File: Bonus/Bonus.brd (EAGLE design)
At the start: 63.5 x 63.5 mm, 63 parts, among them U1 CD4094BPW, U2 CD4094BPW, U3 CD4094BPW, U4 MPU-9250

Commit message: Fixed bug in bonus PCB
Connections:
- net SPI-MISO: now also MSP430.14; no longer MSP430.15
- net SPI-MOSI: now also MSP430.15; no longer MSP430.14
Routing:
- net SPI-CLK: track 17.9 -> 19.2 mm
- net ACCEL-CS: track 22.4 -> 23.7 mm
- net SPI-MOSI: track 13.7 -> 14.7 mm, vias 0 -> 2
- net SPI-MISO: track 21.6 -> 20.9 mm
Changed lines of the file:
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@@
 <?xml version="1.0" encoding="utf-8"?>
 <!DOCTYPE eagle SYSTEM "eagle.dtd">
-<eagle version="8.5.0">
+<eagle version="9.1.2">
 <drawing>
 <settings>
@@
 </class>
 </classes>
-<designrules name="SeeedStudio_2layer_DRU_no_angle_20140221">
+<designrules name="Seeed_DRU">
 <description language="de">&lt;b&gt;EAGLE Design Rules&lt;/b&gt;
 &lt;p&gt;
@@
 <param name="checkStop" value="0"/>
 <param name="checkValues" value="0"/>
+<param name="checkNames" value="1"/>
+<param name="checkWireStubs" value="1"/>
+<param name="checkPolygonWidth" value="0"/>
 <param name="useDiameter" value="13"/>
 <param name="maxErrors" value="50"/>
@@
 <wire x1="30.947" y1="43.983" x2="30.988" y2="43.942" width="0.1524" layer="1"/>
 <wire x1="30.988" y1="43.942" x2="30.988" y2="40.132" width="0.1524" layer="1"/>
-<wire x1="35.052" y1="33.02" x2="34.382" y2="32.35" width="0.1524" layer="1"/>
+<wire x1="36.576" y1="34.544" x2="34.382" y2="32.35" width="0.1524" layer="1"/>
 <wire x1="34.798" y1="39.624" x2="32.258" y2="39.624" width="0.1524" layer="16"/>
 <via x="34.798" y="39.624" extent="1-16" drill="0.35"/>
@@
 <wire x1="30.988" y1="40.132" x2="31.496" y2="39.624" width="0.1524" layer="1"/>
 <wire x1="31.496" y1="39.624" x2="32.258" y2="39.624" width="0.1524" layer="1"/>
-<wire x1="34.798" y1="39.624" x2="35.052" y2="39.37" width="0.1524" layer="1"/>
-<wire x1="35.052" y1="39.37" x2="35.052" y2="33.02" width="0.1524" layer="1"/>
+<wire x1="34.798" y1="39.624" x2="36.576" y2="37.846" width="0.1524" layer="1"/>
+<wire x1="36.576" y1="37.846" x2="36.576" y2="34.544" width="0.1524" layer="1"/>
 </signal>
 <signal name="BUTTON">
@@
 </signal>
 <signal name="SPI-MISO">
-<contactref element="MSP430" pad="15"/>
 <contactref element="U4" pad="9"/>
 <wire x1="30.15" y1="31.95" x2="29.156" y2="31.95" width="0.1524" layer="1"/>
 <wire x1="29.156" y1="31.95" x2="28.956" y2="31.75" width="0.1524" layer="1"/>
 <wire x1="28.956" y1="31.75" x2="27.94" y2="31.75" width="0.1524" layer="1"/>
-<wire x1="35.412" y1="44.633" x2="33.965" y2="44.633" width="0.1524" layer="1"/>
-<wire x1="33.528" y1="38.862" x2="33.528" y2="44.196" width="0.1524" layer="1"/>
-<wire x1="33.965" y1="44.633" x2="33.528" y2="44.196" width="0.1524" layer="1"/>
 <wire x1="27.94" y1="37.592" x2="28.448" y2="38.1" width="0.1524" layer="1"/>
 <wire x1="27.94" y1="31.75" x2="27.94" y2="37.592" width="0.1524" layer="1"/>
 <wire x1="32.766" y1="38.1" x2="33.528" y2="38.862" width="0.1524" layer="1"/>
 <wire x1="28.448" y1="38.1" x2="32.766" y2="38.1" width="0.1524" layer="1"/>
+<contactref element="MSP430" pad="14"/>
+<wire x1="33.528" y1="43.434" x2="33.528" y2="38.862" width="0.1524" layer="1"/>
+<wire x1="35.412" y1="43.983" x2="34.077" y2="43.983" width="0.1524" layer="1"/>
+<wire x1="34.077" y1="43.983" x2="33.528" y2="43.434" width="0.1524" layer="1"/>
 </signal>
 <signal name="SPI-MOSI">
-<contactref element="MSP430" pad="14"/>
 <contactref element="U4" pad="24"/>
 <wire x1="33.35" y1="32.75" x2="34.02" y2="32.75" width="0.1524" layer="1"/>
-<wire x1="34.544" y1="33.274" x2="34.02" y2="32.75" width="0.1524" layer="1"/>
-<wire x1="35.412" y1="43.983" x2="34.077" y2="43.983" width="0.1524" layer="1"/>
-<wire x1="34.077" y1="43.983" x2="34.036" y2="43.942" width="0.1524" layer="1"/>
-<wire x1="34.036" y1="43.942" x2="34.036" y2="38.608" width="0.1524" layer="1"/>
-<wire x1="34.036" y1="38.608" x2="34.544" y2="38.1" width="0.1524" layer="1"/>
-<wire x1="34.544" y1="38.1" x2="34.544" y2="33.274" width="0.1524" layer="1"/>
+<contactref element="MSP430" pad="15"/>
+<wire x1="35.412" y1="44.633" x2="36.139" y2="44.633" width="0.1524" layer="1"/>
+<wire x1="36.139" y1="44.633" x2="36.83" y2="43.942" width="0.1524" layer="1"/>
+<wire x1="36.83" y1="43.18" x2="36.83" y2="43.942" width="0.1524" layer="16"/>
+<via x="36.83" y="43.942" extent="1-16" drill="0.35"/>
+<wire x1="35.56" y1="37.084" x2="36.068" y2="37.592" width="0.1524" layer="16"/>
+<via x="35.56" y="37.084" extent="1-16" drill="0.35"/>
+<wire x1="35.56" y1="34.29" x2="35.56" y2="37.084" width="0.1524" layer="1"/>
+<wire x1="34.02" y1="32.75" x2="35.56" y2="34.29" width="0.1524" layer="1"/>
+<wire x1="36.068" y1="37.592" x2="36.068" y2="37.592" width="0.1524" layer="16"/>
+<wire x1="36.068" y1="37.592" x2="36.068" y2="42.418" width="0.1524" layer="16"/>
+<wire x1="36.068" y1="42.418" x2="36.83" y2="43.18" width="0.1524" layer="16"/>
 </signal>
 <signal name="N$7">
@@
 <contactref element="MSP430" pad="19"/>
 <wire x1="35.412" y1="47.2329" x2="34.0249" y2="47.2329" width="0.1524" layer="1"/>
-<wire x1="34.998" y1="31.95" x2="35.56" y2="32.512" width="0.1524" layer="1"/>
-<wire x1="35.56" y1="40.64" x2="35.306" y2="40.894" width="0.1524" layer="1"/>
+<wire x1="34.998" y1="31.95" x2="37.084" y2="34.036" width="0.1524" layer="1"/>
+<wire x1="37.084" y1="39.116" x2="35.306" y2="40.894" width="0.1524" layer="1"/>
 <wire x1="35.306" y1="40.894" x2="32.258" y2="40.894" width="0.1524" layer="16"/>
-<wire x1="35.56" y1="32.512" x2="35.56" y2="40.64" width="0.1524" layer="1"/>
 <via x="35.306" y="40.894" extent="1-16" drill="0.35"/>
 <via x="32.258" y="40.894" extent="1-16" drill="0.35"/>
+<wire x1="37.084" y1="34.036" x2="37.084" y2="39.116" width="0.1524" layer="1"/>
 <wire x1="32.258" y1="45.466" x2="32.258" y2="40.894" width="0.1524" layer="1"/>
 <wire x1="34.0249" y1="47.2329" x2="32.258" y2="45.466" width="0.1524" layer="1"/>
@@
 </signal>
 </signals>
+<mfgpreviewcolors>
+<mfgpreviewcolor name="soldermaskcolor" color="0xC8008000"/>
+<mfgpreviewcolor name="silkscreencolor" color="0xFFFEFEFE"/>
+<mfgpreviewcolor name="backgroundcolor" color="0xFF282828"/>
+<mfgpreviewcolor name="coppercolor" color="0xFFFFBF00"/>
+<mfgpreviewcolor name="substratecolor" color="0xFF786E46"/>
+</mfgpreviewcolors>
 </board>
 </drawing>

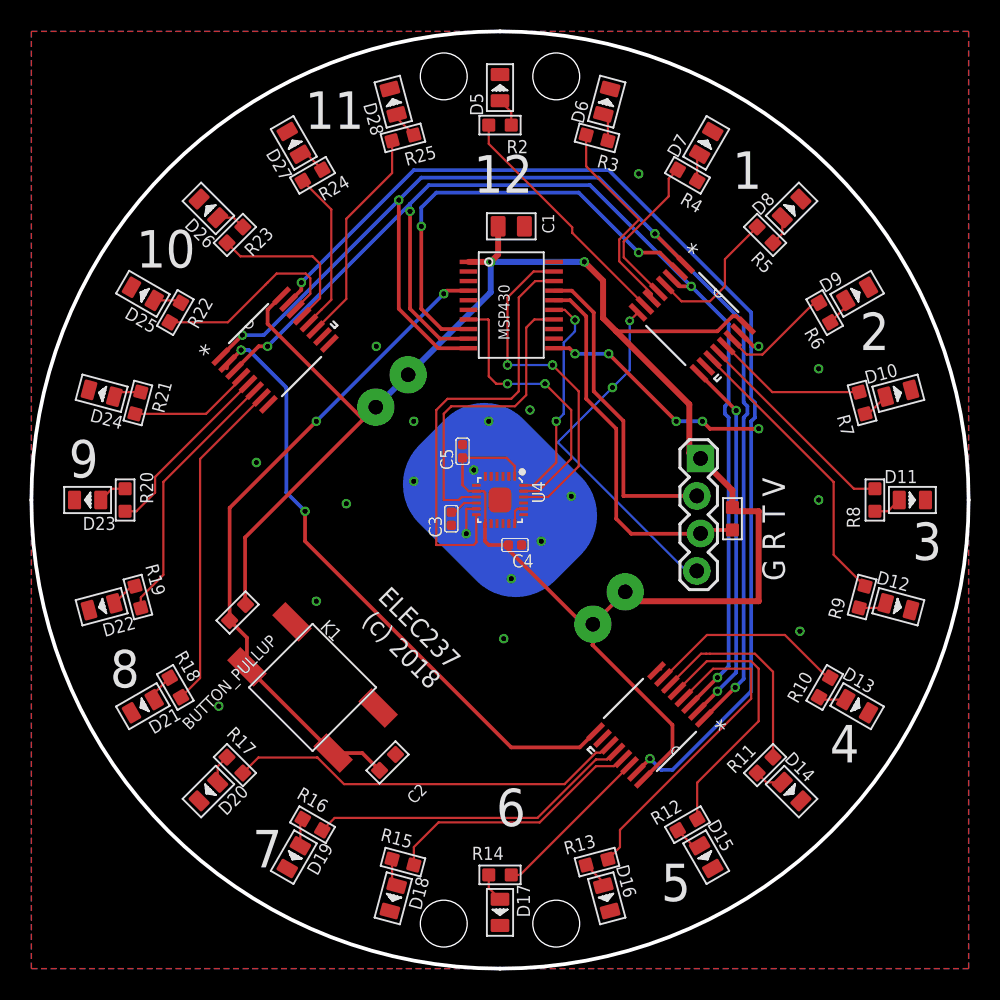
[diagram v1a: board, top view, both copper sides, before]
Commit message: Updated LED resistors from 1K to 300 ohms
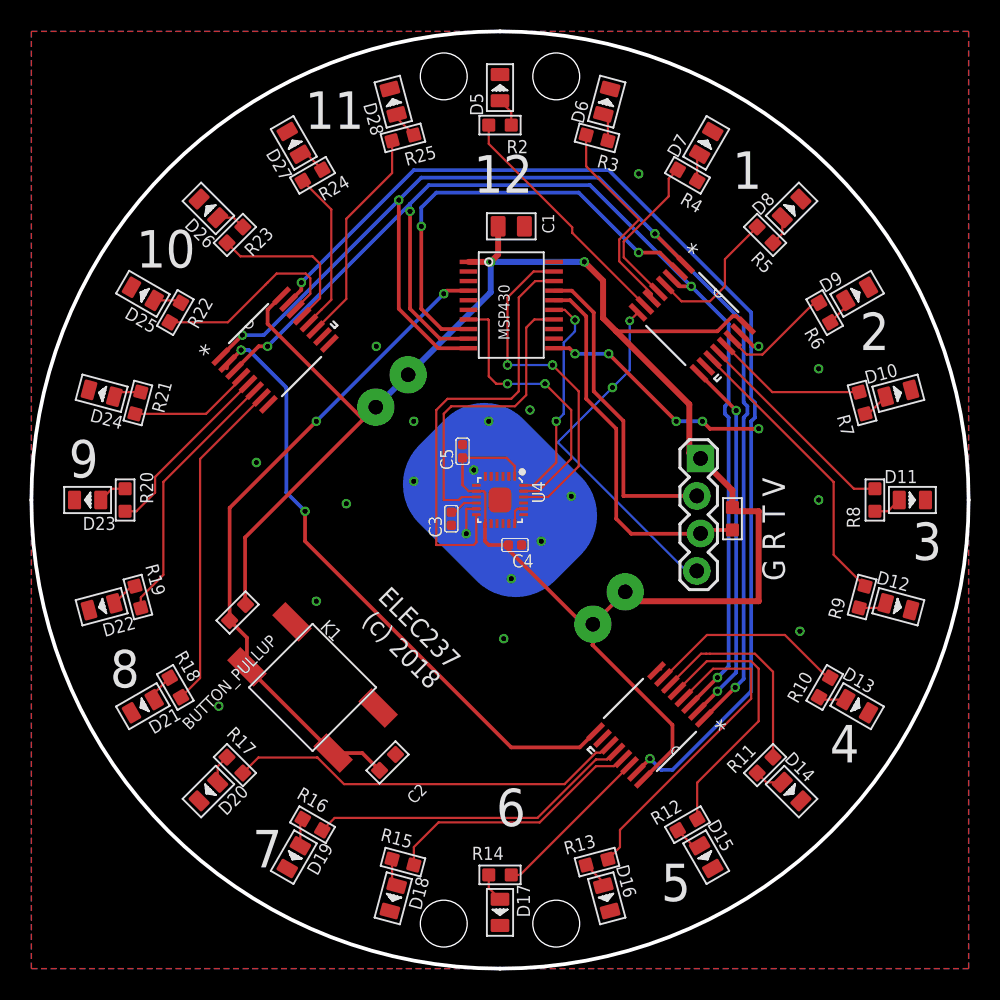
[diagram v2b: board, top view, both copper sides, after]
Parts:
- R10, R11, R12, R13, R14, R15, R16, R17, R18, R19, R2, R20, R21, R22, R23, R24, R25, R3, R4, R5, R6, R7, R8, R9: value 1K 1/10W -> 300 1/10W

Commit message: Moved Lab3 to Lab4 and added new RGB LED. Also updated Bonus PCB for manufacturing
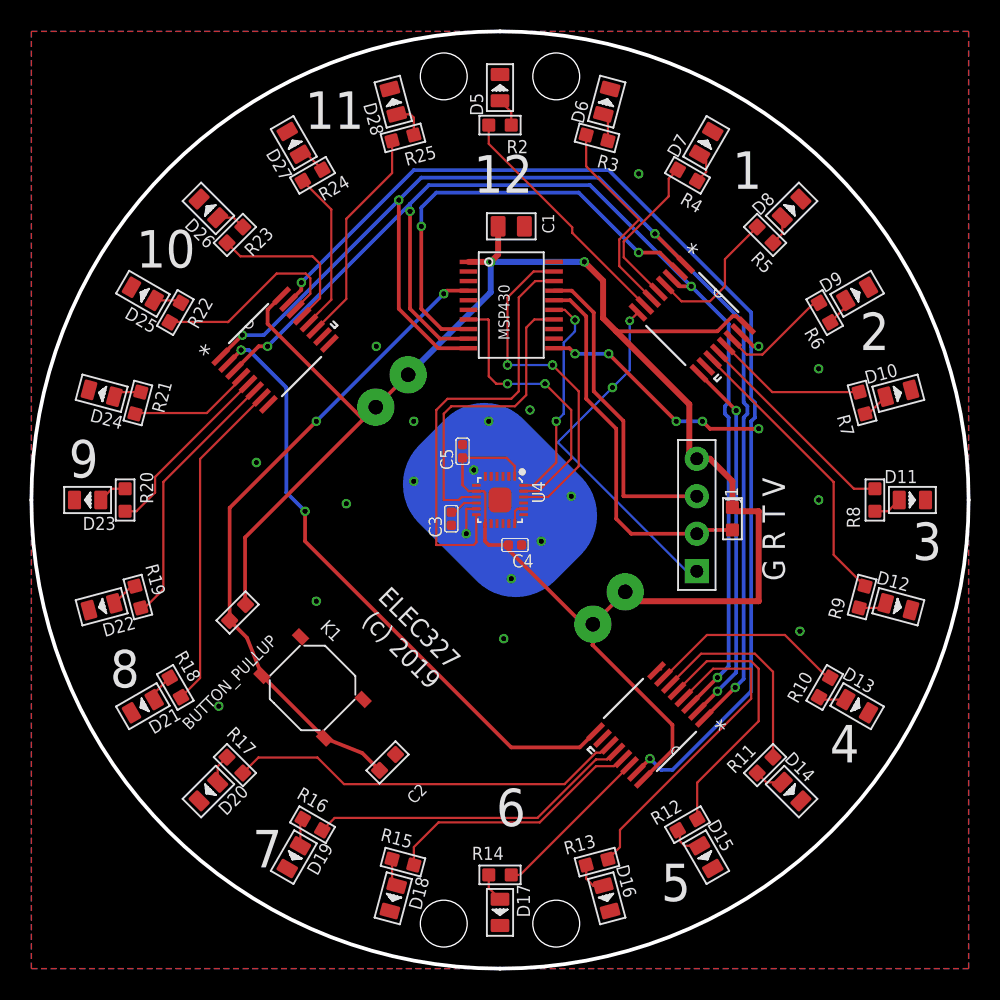
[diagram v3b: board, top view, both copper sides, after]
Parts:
- removed JP1: (no value), Pendant:1X04_LOCK
- added J1: 4p-2.54, OPL_Connector:H4-2.54
- BAT1: value 20mm coincell -> BAT-HLD-001-THM-ND 20 mm Coin Cell
- C2: value 470nf -> 220nf; device Seeed-OPL-Capacitor:C0603 -> OPL_Capacitor:C0603
- K1: value (none) -> SKQGADE010; device Seeed-OPL-Switch:SW4-SMD-6.0X6.0X5.0MM -> OPL_Switch:SW4-SMD-5.2X5.2X1.5MM
- R10, R11, R12, R13, R14, R15, R16, R17, R18, R19, R2, R20, R21, R22, R23, R24, R25, R3, R4, R5, R6, R7, R8, R9: value 300 1/10W -> 390R; device Seeed-OPL-Resistor:R0603 -> OPL_Resistor:R0603
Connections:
- net BUTTON: now also K1.4; no longer K1.2
- net GND: now also J1.1, K1.2; no longer JP1.4, K1.4
- net TEST: now also J1.3; no longer JP1.2
- net VDD: now also J1.4; no longer JP1.1
- net _RST: now also J1.2; no longer JP1.3
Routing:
- net _RST: track 26.5 -> 25.6 mm
- net N$21: track 1.92 -> 2.70 mm
- net GND: track 28.4 -> 27.7 mm
- net BUTTON: track 45.4 -> 44.7 mm
- net D9: track 14.8 -> 14.1 mm
- net N$22: track 1.88 -> 2.51 mm
- net N$3: track 1.88 -> 2.48 mm
- net N$34: track 1.88 -> 2.46 mm
- net D1: track 14.6 -> 14.0 mm
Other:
- board text added: "ELEC327 (c) 2019"
- board text removed: "ELEC237 (c) 2018"
